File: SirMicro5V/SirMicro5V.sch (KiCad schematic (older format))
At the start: 31 parts, among them J1 Conn_01x16, J2 Conn_01x16, J3 USB_B_Micro, U1 ATmega32U4-AU, U2 AP2127K-3.3, Y1 Resonator

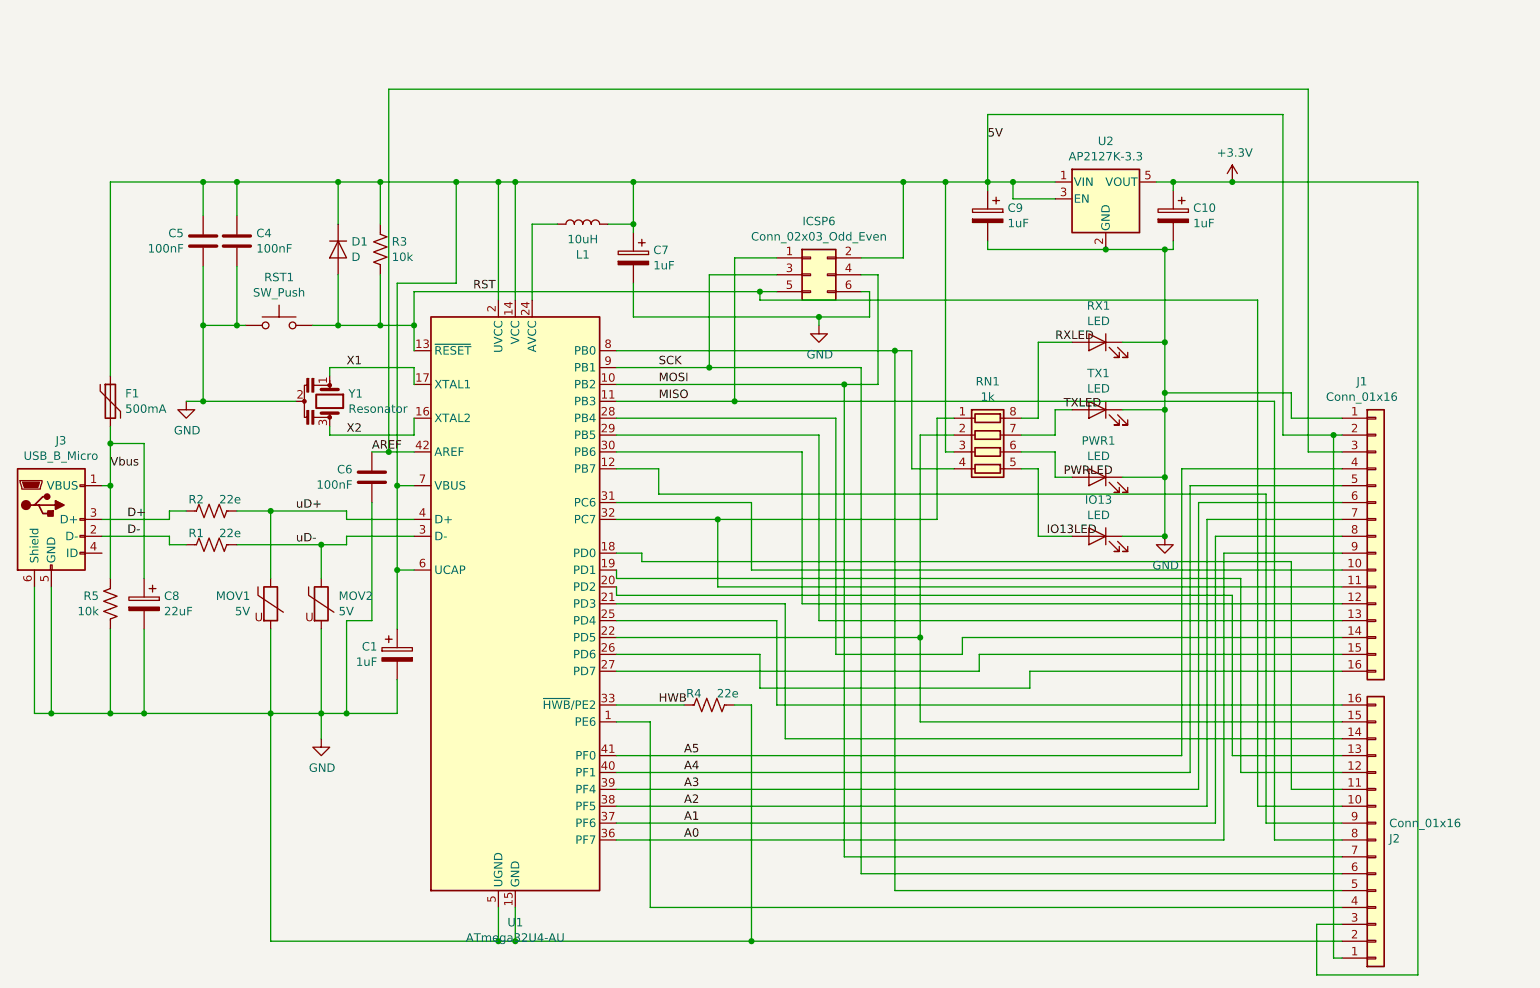
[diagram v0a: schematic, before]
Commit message: PCB silkscreen revised
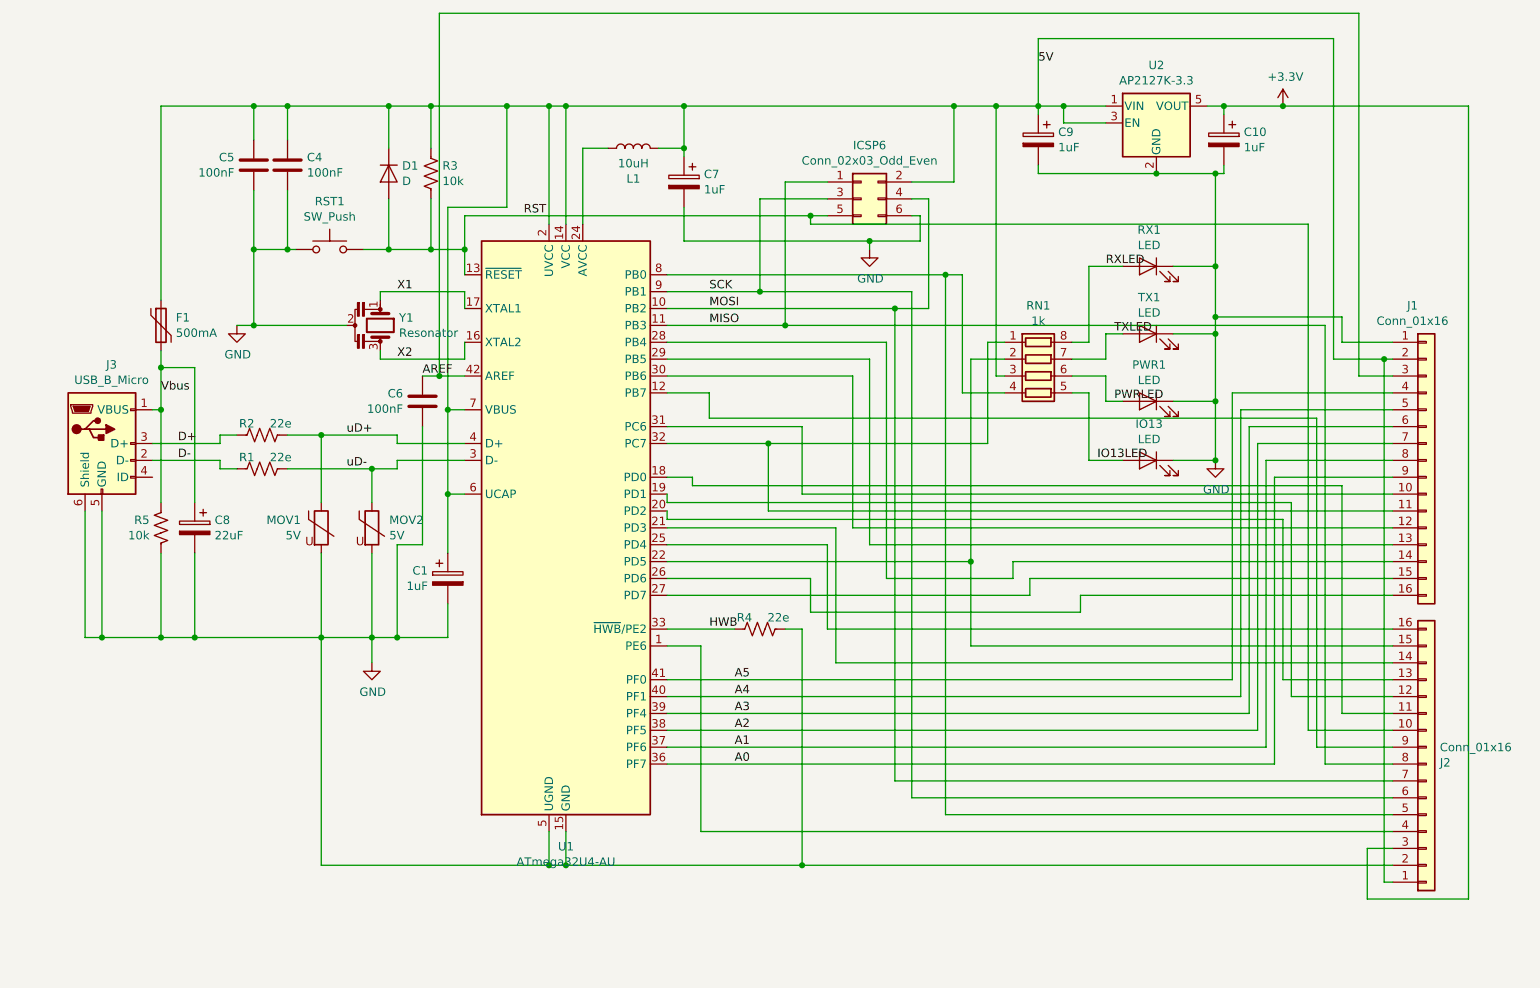
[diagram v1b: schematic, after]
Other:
- moved on the sheet: C1, C10, C4, C5, C6, C7, C8, C9, D1, F1, ICSP6, IO13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

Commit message: Board Layout Revised and 3V3 Version Added
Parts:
- added JP1: SolderJumper_2_Bridged, Jumper:SolderJumper-2_P1.3mm_Bridged_RoundedPad1.0x1.5mm, symbol Jumper:SolderJumper_2_Bridged
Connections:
- net labels added: 3V3, D10, D11, D12, D13, D4, D5, D6, D7, D8, D9, RX, SCL, SDA, TX
- net labels removed: +3.3V, IO13LED, PWRLED
- wire segments 273 -> 200
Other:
- moved on the sheet: C10, C9, ICSP6, IO13, J1, J2, PWR1, RN1, RX1, TX1, U2

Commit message: Dual Voltage And Voltage Selector Added, QFN Package used
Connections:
- wire segments 200 -> 199
